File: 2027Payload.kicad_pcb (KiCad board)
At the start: 4 copper layers, 60 x 90 mm, 96 parts, among them J1 USB_C_Receptacle_USB2.0_16P, J10 Conn_02x03_Odd_Even, J11 Conn_01x03, J2 Conn_01x01, J3 Conn_01x03, J4 Conn_01x03, J5 Conn_01x03, J6 Conn_01x04, J7 Conn_01x04, J8 Conn_01x04, J9 Conn_01x01, Q2 AO4407A, SW1 SW_Push, SW2 SW_Push, U1 ESP32-S3-WROOM-1-N8R8, U11 SAM-M10Q-00B, U12 BMP581, U2 TPS543620RPYR, U3 TPS22965DSGT, U4 BNO085, U6 USBLC6-2SC6, U7 TLV75533PDBVR, U9 TPS2113ADRBR

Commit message: Added pins for one extra servo.
5V, GND, IO14
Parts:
- added J12: Conn_01x03, Connector_PinHeader_2.54mm:PinHeader_1x03_P2.54mm_Vertical, F.Cu at (223.0, 150.0)
- added R37: 330R, Capacitor_SMD:C_0603_1608Metric, F.Cu at (222.0, 147.2)
- C40: value 220u -> 22u
- C44: value 100u -> 22u
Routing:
- net IO14: track 0.00 -> 69.9 mm, vias 0 -> 2
- net Net-(J12-Pin_1): track 0.00 -> 2.81 mm

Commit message: Final BOM
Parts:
- R10, R14, R15, R16, R17, R18, R19, R20, R21, R22, R23, R24, R25, R26, R27, R28, R29, R30, R31, R32, R33, R34, R35, R36, R37, R7, R8, R9: footprint Capacitor_SMD:C_0603_1608Metric -> Resistor_SMD:R_0603_1608Metric

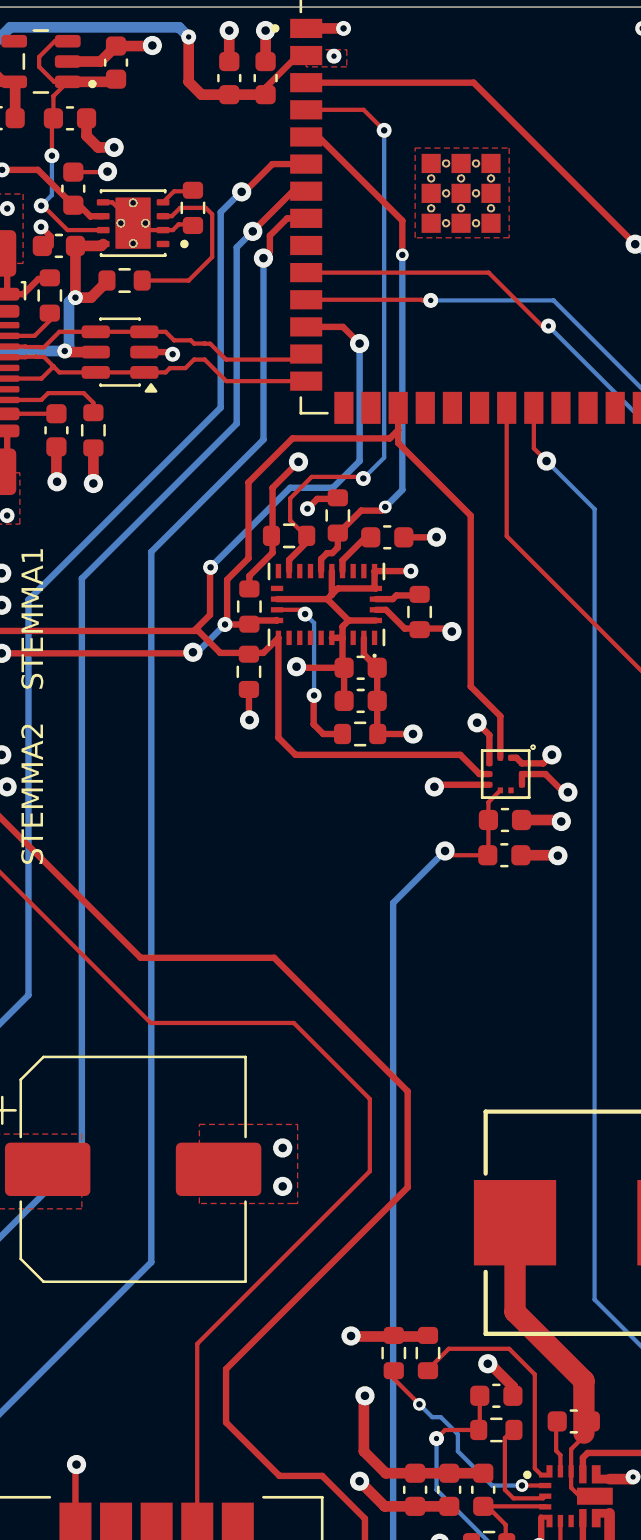
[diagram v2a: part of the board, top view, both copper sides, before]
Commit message: BNO085 --> BNO055
Due to stock issues, the BNO085 was changed to a BNO055.

*Updated gerber, drill, pos files (IN ZIP FILE IN MANUFACTURING > 2027Payload_GBR_DRL_POS_V5)
*Updated schematic and PCB design
*Updated BOM
*Updated canva block diagrams
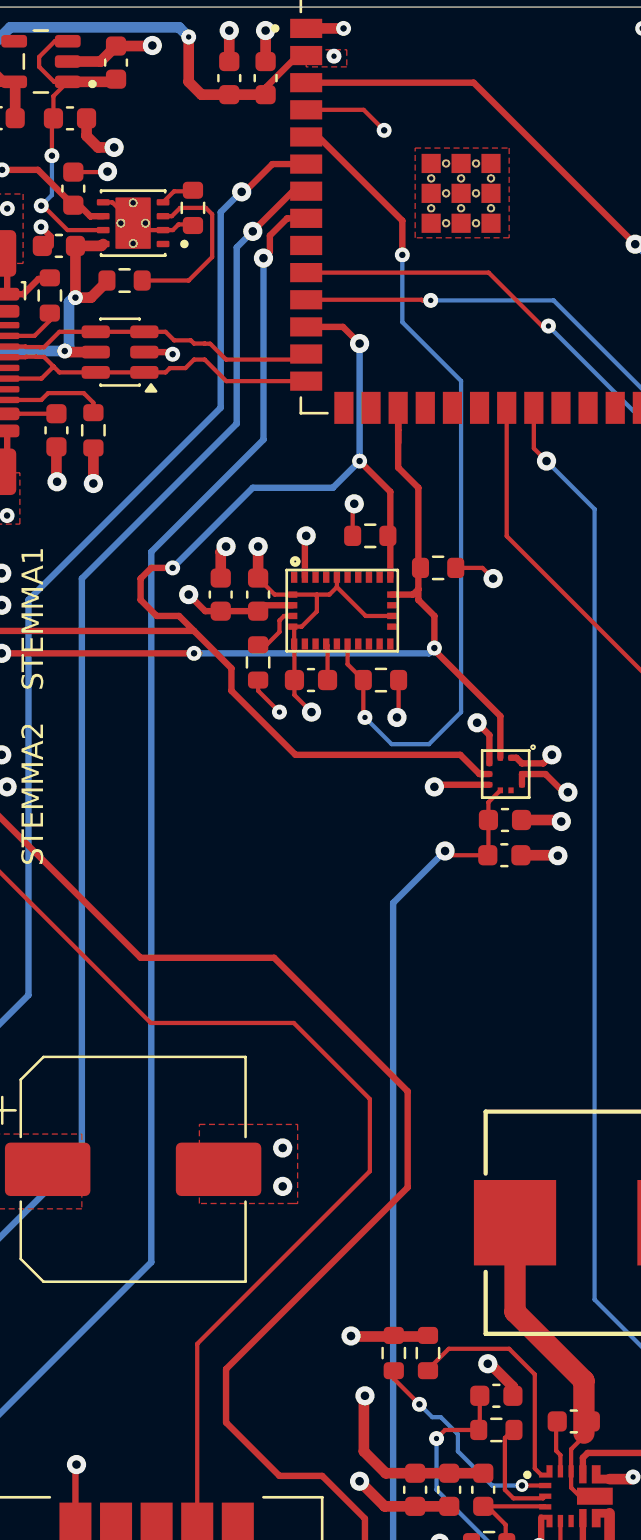
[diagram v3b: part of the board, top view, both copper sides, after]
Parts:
- removed C19, C20, C21: 100n, Capacitor_SMD:C_0603_1608Metric
- removed R14, R19, R20: 10k, Resistor_SMD:R_0603_1608Metric
- removed R17, R18: 4.7k, Resistor_SMD:R_0603_1608Metric
- removed U4: BNO085, BNO085:IC_BNO085
- added C47: 100n, Capacitor_SMD:C_0603_1608Metric, F.Cu at (200.2, 89.5)
- added C48: 100n, Capacitor_SMD:C_0603_1608Metric, F.Cu at (198.5, 89.5)
- added C49: 100n, Capacitor_SMD:C_0603_1608Metric, F.Cu at (202.7, 93.5)
- added R38: 10k, Resistor_SMD:R_0603_1608Metric, F.Cu at (200.2, 92.7)
- added R39: 10k, Resistor_SMD:R_0603_1608Metric, F.Cu at (205.5, 86.8)
- added R40: 10k, Resistor_SMD:R_0603_1608Metric, F.Cu at (208.7, 88.2)
- added U5: BNO055, BNO055:LGA28R50P4X10_380X520X100, F.Cu at (204.2, 90.2)
- moved R29 2.71 mm to (206.0, 93.5)
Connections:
- R29 pad 2: Net-(U4-~{H_CS}) -> IO5
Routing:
- net IO4: track 28.7 -> 4.05 mm, vias 2 -> 1
- net IO5: track 24.9 -> 39.7 mm
- net Net-(U4-~{H_CS}): track 8.33 -> 0.00 mm, vias 2 -> 0
- net IO8: track 123.6 -> 131.3 mm, vias 2 -> 3
- net +3.3V: track 136.4 -> 130.4 mm, vias 14 -> 15
- net IO9: track 108.9 -> 103.8 mm
- net Net-(U5-NBOOT_LOAD_PIN): track 0.00 -> 2.50 mm
- net Net-(U4-CAP): track 2.27 -> 0.00 mm
- net Net-(U4-~{BOOT}): track 2.12 -> 0.00 mm
- net GND: track 175.0 -> 173.0 mm
- net Net-(U5-CAP): track 0.00 -> 1.71 mm
